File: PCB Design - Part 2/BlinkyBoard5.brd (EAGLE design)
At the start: 100 x 80 mm, 10 parts, among them IC1 LM555D

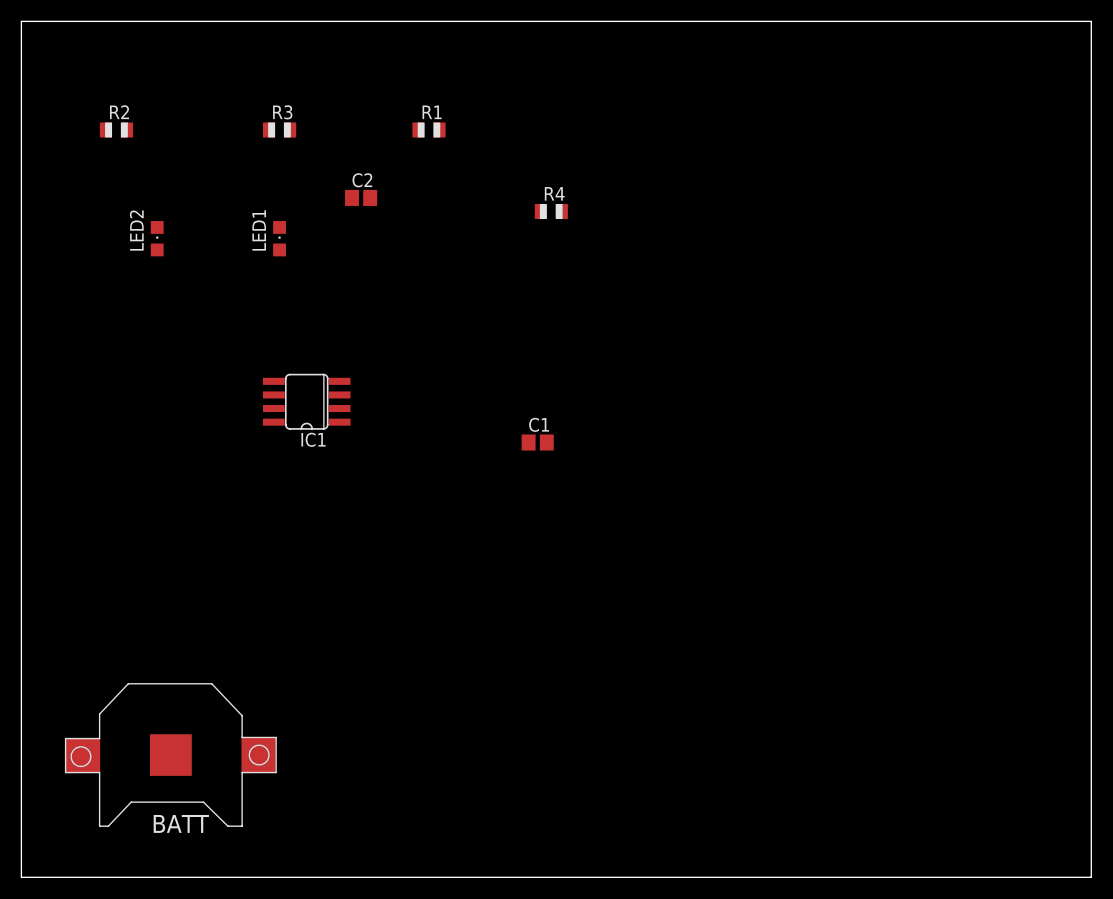
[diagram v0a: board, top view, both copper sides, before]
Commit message: Added components onto PCB
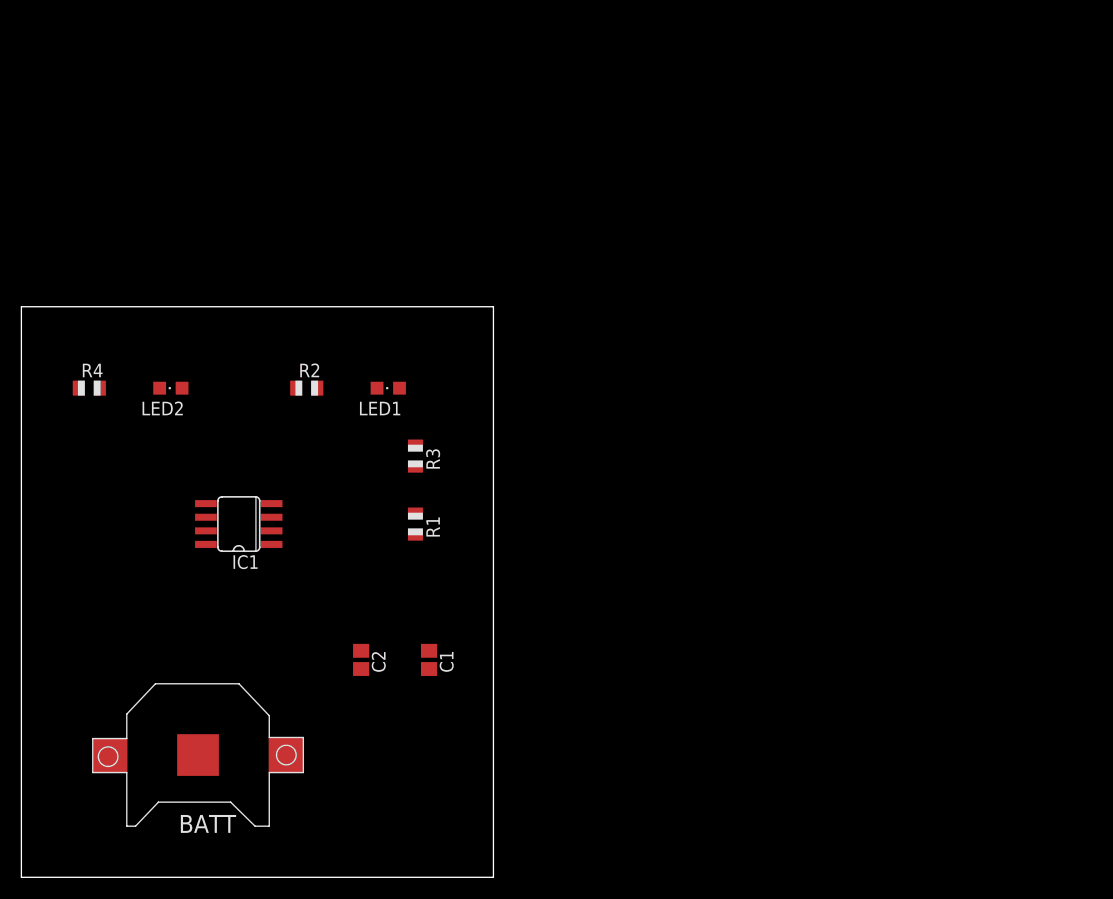
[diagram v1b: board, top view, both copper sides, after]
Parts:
- moved R4 46.2 mm to (6.35, 45.7)
- moved C2 43.2 mm to (31.8, 20.3), turned to 270 degrees
- moved R1 36.9 mm to (36.8, 33.0), turned to 270 degrees
- moved R3 33.0 mm to (36.8, 39.4), turned to 270 degrees
- moved R2 30.0 mm to (26.7, 45.7)
- moved C1 22.7 mm to (38.1, 20.3), turned to 270 degrees
- moved LED1 17.3 mm to (34.3, 45.7), turned to 90 degrees
- moved LED2 14.0 mm to (14.0, 45.7), turned to 90 degrees
- moved IC1 13.1 mm to (20.3, 33.0)
- moved BATT 2.54 mm to (16.5, 11.4)
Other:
- board size 100 x 80 mm -> 44.1 x 53.3 mm
